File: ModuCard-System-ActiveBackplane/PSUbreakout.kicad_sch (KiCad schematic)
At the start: 16 parts

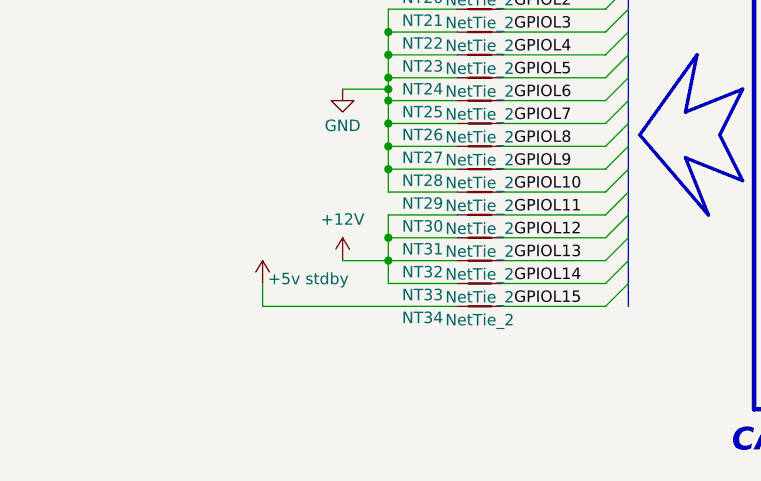
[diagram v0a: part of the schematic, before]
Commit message: [3] Rebalance power rails
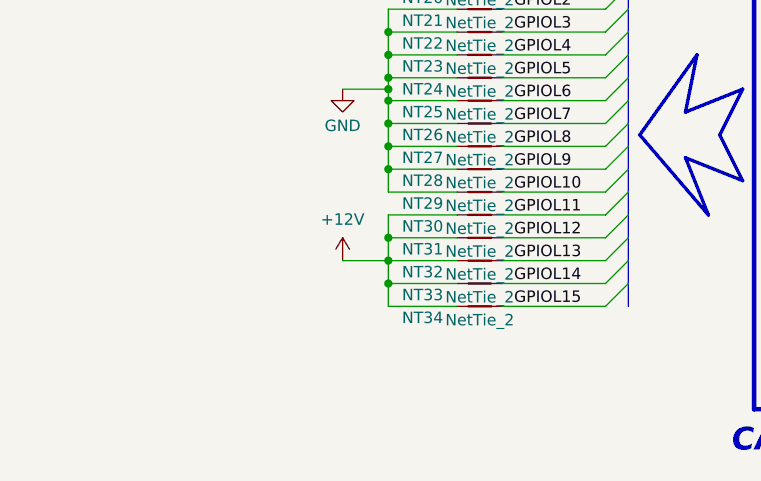
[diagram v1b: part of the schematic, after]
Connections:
- net +5v stdby is gone; now on net +12V: NT34.1
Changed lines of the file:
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@@
 	)
 	(junction
+		(at 78.74 121.92)
+		(diameter 0)
+		(color 0 0 0 0)
+	)
+	(junction
 		(at 78.74 87.63)
 		(diameter 0)
@@
 	(wire
 		(pts
-			(xy 64.77 124.46) (xy 86.36 124.46)
-		)
-		(stroke
-			(width 0)
-			(type default)
-		)
-	)
-	(wire
-		(pts
 			(xy 78.74 86.36) (xy 78.74 87.63)
 		)
@@
 	(wire
 		(pts
-			(xy 64.77 124.46) (xy 64.77 121.92)
-		)
-		(stroke
-			(width 0)
-			(type default)
-		)
-	)
-	(wire
-		(pts
 			(xy 78.74 99.06) (xy 86.36 99.06)
 		)
@@
 	(wire
 		(pts
+			(xy 86.36 124.46) (xy 78.74 124.46)
+		)
+		(stroke
+			(width 0)
+			(type default)
+		)
+	)
+	(wire
+		(pts
+			(xy 78.74 124.46) (xy 78.74 121.92)
+		)
+		(stroke
+			(width 0)
+			(type default)
+		)
+	)
+	(wire
+		(pts
 			(xy 91.44 111.76) (xy 102.87 111.76)
 		)
@@
 					(unit 1)
 				)
-			)
-		)
-	)
-	(symbol
-		(lib_id "power:+12V")
-		(at 64.77 121.92 0)
-		(mirror y)
-		(unit 1)
-		(exclude_from_sim no)
-		(in_bom yes)
-		(on_board yes)
-		(dnp no)
-		(property "Reference" "#PWR011"
-			(at 64.77 125.73 0)
-			(effects
-				(font
-					(size 1.27 1.27)
-				)
-				(hide yes)
-			)
-		)
-		(property "Value" "+5v stdby"
-			(at 69.85 121.412 0)
-			(effects
-				(font
-					(size 1.27 1.27)
-				)
-			)
-		)
-		(property "Footprint" ""
-			(at 64.77 121.92 0)
-			(effects
-				(font
-					(size 1.27 1.27)
-				)
-				(hide yes)
-			)
-		)
-		(property "Datasheet" ""
-			(at 64.77 121.92 0)
-			(effects
-				(font
-					(size 1.27 1.27)
-				)
-				(hide yes)
-			)
-		)
-		(property "Description" "Power symbol creates a global label with name \"+12V\""
-			(at 64.77 121.92 0)
-			(effects
-				(font
-					(size 1.27 1.27)
-				)
-				(hide yes)
-			)
-		)
-		(pin "1"
-		)
-		(instances
-			(project "ModuCard-System-ActiveBackplane"
-				(path "/8ab7bab9-e078-4eba-84b5-91e80d010216/fe6b9307-b057-4908-8958-4420dfd82621"
-					(reference "#PWR011")
-					(unit 1)
-				)

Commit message: [2][5] Aplly layout finishing touches
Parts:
- renumbered NT26 to NT10, NT27 to NT11, NT28 to NT12, NT29 to NT13, NT30 to NT14, NT31 to NT15, NT32 to NT16, NT33 to NT17, NT34 to NT18, NT19 to NT3, NT20 to NT4, NT21 to NT5, NT22 to NT6, NT23 to NT7, NT24 to NT8, NT25 to NT9
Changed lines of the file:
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@@
 		(on_board yes)
 		(dnp no)
-		(property "Reference" "NT21"
+		(property "Reference" "NT5"
 			(at 82.55 92.71 0)
 			(effects
@@
 			(project "ModuCard-System-ActiveBackplane"
 				(path "/8ab7bab9-e078-4eba-84b5-91e80d010216/fe6b9307-b057-4908-8958-4420dfd82621"
-					(reference "NT21")
+					(reference "NT5")
 					(unit 1)
 				)
@@
 		(on_board yes)
 		(dnp no)
-		(property "Reference" "NT26"
+		(property "Reference" "NT10"
 			(at 82.55 105.41 0)
 			(effects
@@
 			(project "ModuCard-System-ActiveBackplane"
 				(path "/8ab7bab9-e078-4eba-84b5-91e80d010216/fe6b9307-b057-4908-8958-4420dfd82621"
-					(reference "NT26")
+					(reference "NT10")
 					(unit 1)
 				)
@@
 		(on_board yes)
 		(dnp no)
-		(property "Reference" "#PWR0633"
+		(property "Reference" "#PWR0486"
 			(at 73.66 106.68 0)
 			(effects
@@
 			(project "ModuCard-System-ActiveBackplane"
 				(path "/8ab7bab9-e078-4eba-84b5-91e80d010216/fe6b9307-b057-4908-8958-4420dfd82621"
-					(reference "#PWR0633")
+					(reference "#PWR0486")
 					(unit 1)
 				)
@@
 		(on_board yes)
 		(dnp no)
-		(property "Reference" "NT25"
+		(property "Reference" "NT9"
 			(at 82.55 102.87 0)
 			(effects
@@
 			(project "ModuCard-System-ActiveBackplane"
 				(path "/8ab7bab9-e078-4eba-84b5-91e80d010216/fe6b9307-b057-4908-8958-4420dfd82621"
-					(reference "NT25")
+					(reference "NT9")
 					(unit 1)
 				)
@@
 		(on_board yes)
 		(dnp no)
-		(property "Reference" "NT32"
+		(property "Reference" "NT16"
 			(at 82.55 120.65 0)
 			(effects
@@
 			(project "ModuCard-System-ActiveBackplane"
 				(path "/8ab7bab9-e078-4eba-84b5-91e80d010216/fe6b9307-b057-4908-8958-4420dfd82621"
-					(reference "NT32")
+					(reference "NT16")
 					(unit 1)
 				)
@@
 		(on_board yes)
 		(dnp no)
-		(property "Reference" "NT30"
+		(property "Reference" "NT14"
 			(at 82.55 115.57 0)
 			(effects
@@
 			(project "ModuCard-System-ActiveBackplane"
 				(path "/8ab7bab9-e078-4eba-84b5-91e80d010216/fe6b9307-b057-4908-8958-4420dfd82621"
-					(reference "NT30")
+					(reference "NT14")
 					(unit 1)
 				)
@@
 		(on_board yes)
 		(dnp no)
-		(property "Reference" "#PWR0632"
+		(property "Reference" "#PWR0485"
 			(at 73.66 91.44 0)
 			(effects
@@
 			(project "ModuCard-System-ActiveBackplane"
 				(path "/8ab7bab9-e078-4eba-84b5-91e80d010216/fe6b9307-b057-4908-8958-4420dfd82621"
-					(reference "#PWR0632")
+					(reference "#PWR0485")
 					(unit 1)
 				)
@@
 		(on_board yes)
 		(dnp no)
-		(property "Reference" "NT19"
+		(property "Reference" "NT3"
 			(at 82.55 87.63 0)
 			(effects
@@
 			(project "ModuCard-System-ActiveBackplane"
 				(path "/8ab7bab9-e078-4eba-84b5-91e80d010216/fe6b9307-b057-4908-8958-4420dfd82621"
-					(reference "NT19")
+					(reference "NT3")
 					(unit 1)
 				)
@@
 		(on_board yes)
 		(dnp no)
-		(property "Reference" "NT31"
+		(property "Reference" "NT15"
 			(at 82.55 118.11 0)
 			(effects
@@
 			(project "ModuCard-System-ActiveBackplane"
 				(path "/8ab7bab9-e078-4eba-84b5-91e80d010216/fe6b9307-b057-4908-8958-4420dfd82621"
-					(reference "NT31")
+					(reference "NT15")
 					(unit 1)
 				)
@@
 		(on_board yes)
 		(dnp no)
-		(property "Reference" "NT34"
+		(property "Reference" "NT18"
 			(at 82.55 125.73 0)
 			(effects
@@
 			(project "ModuCard-System-ActiveBackplane"
 				(path "/8ab7bab9-e078-4eba-84b5-91e80d010216/fe6b9307-b057-4908-8958-4420dfd82621"
-					(reference "NT34")
+					(reference "NT18")
 					(unit 1)
 				)
@@
 		(on_board yes)
 		(dnp no)
-		(property "Reference" "NT22"
+		(property "Reference" "NT6"
 			(at 82.55 95.25 0)
 			(effects
@@
 			(project "ModuCard-System-ActiveBackplane"
 				(path "/8ab7bab9-e078-4eba-84b5-91e80d010216/fe6b9307-b057-4908-8958-4420dfd82621"
-					(reference "NT22")
+					(reference "NT6")
 					(unit 1)
 				)
@@
 		(on_board yes)
 		(dnp no)
-		(property "Reference" "NT29"
+		(property "Reference" "NT13"
 			(at 82.55 113.03 0)
 			(effects
@@
 			(project "ModuCard-System-ActiveBackplane"
 				(path "/8ab7bab9-e078-4eba-84b5-91e80d010216/fe6b9307-b057-4908-8958-4420dfd82621"
-					(reference "NT29")
+					(reference "NT13")
 					(unit 1)
 				)
@@
 		(on_board yes)
 		(dnp no)
-		(property "Reference" "NT24"
+		(property "Reference" "NT8"
 			(at 82.55 100.33 0)
 			(effects
@@
 			(project "ModuCard-System-ActiveBackplane"
 				(path "/8ab7bab9-e078-4eba-84b5-91e80d010216/fe6b9307-b057-4908-8958-4420dfd82621"
-					(reference "NT24")
+					(reference "NT8")
 					(unit 1)
 				)
@@
 		(on_board yes)
 		(dnp no)
-		(property "Reference" "NT20"
+		(property "Reference" "NT4"
 			(at 82.55 90.17 0)
 			(effects
@@
 			(project "ModuCard-System-ActiveBackplane"
 				(path "/8ab7bab9-e078-4eba-84b5-91e80d010216/fe6b9307-b057-4908-8958-4420dfd82621"
-					(reference "NT20")
+					(reference "NT4")
 					(unit 1)
 				)
@@
 		(on_board yes)
 		(dnp no)
-		(property "Reference" "#PWR0575"
+		(property "Reference" "#PWR0487"
 			(at 73.66 123.19 0)
 			(effects
@@
 			(project "ModuCard-System-ActiveBackplane"
 				(path "/8ab7bab9-e078-4eba-84b5-91e80d010216/fe6b9307-b057-4908-8958-4420dfd82621"
-					(reference "#PWR0575")
+					(reference "#PWR0487")
 					(unit 1)
 				)
@@
 		(on_board yes)
 		(dnp no)
-		(property "Reference" "NT28"
+		(property "Reference" "NT12"
 			(at 82.55 110.49 0)
 			(effects
@@
 			(project "ModuCard-System-ActiveBackplane"
 				(path "/8ab7bab9-e078-4eba-84b5-91e80d010216/fe6b9307-b057-4908-8958-4420dfd82621"
-					(reference "NT28")
+					(reference "NT12")
 					(unit 1)
 				)
@@
 		(on_board yes)
 		(dnp no)
-		(property "Reference" "NT27"
+		(property "Reference" "NT11"
 			(at 82.55 107.95 0)
 			(effects
@@
 			(project "ModuCard-System-ActiveBackplane"
 				(path "/8ab7bab9-e078-4eba-84b5-91e80d010216/fe6b9307-b057-4908-8958-4420dfd82621"
-					(reference "NT27")
+					(reference "NT11")
 					(unit 1)
 				)
@@
 		(on_board yes)
 		(dnp no)
-		(property "Reference" "NT23"
+		(property "Reference" "NT7"
 			(at 82.55 97.79 0)
 			(effects
@@
 			(project "ModuCard-System-ActiveBackplane"
 				(path "/8ab7bab9-e078-4eba-84b5-91e80d010216/fe6b9307-b057-4908-8958-4420dfd82621"
-					(reference "NT23")
+					(reference "NT7")
 					(unit 1)
 				)
@@
 		(on_board yes)
 		(dnp no)
-		(property "Reference" "NT33"
+		(property "Reference" "NT17"
 			(at 82.55 123.19 0)
 			(effects
@@
 			(project "ModuCard-System-ActiveBackplane"
 				(path "/8ab7bab9-e078-4eba-84b5-91e80d010216/fe6b9307-b057-4908-8958-4420dfd82621"
-					(reference "NT33")
-					(unit 1)
-				)
+					(reference "NT17")
+					(unit 1)
+				)
